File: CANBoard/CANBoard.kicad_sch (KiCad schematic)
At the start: 26 parts

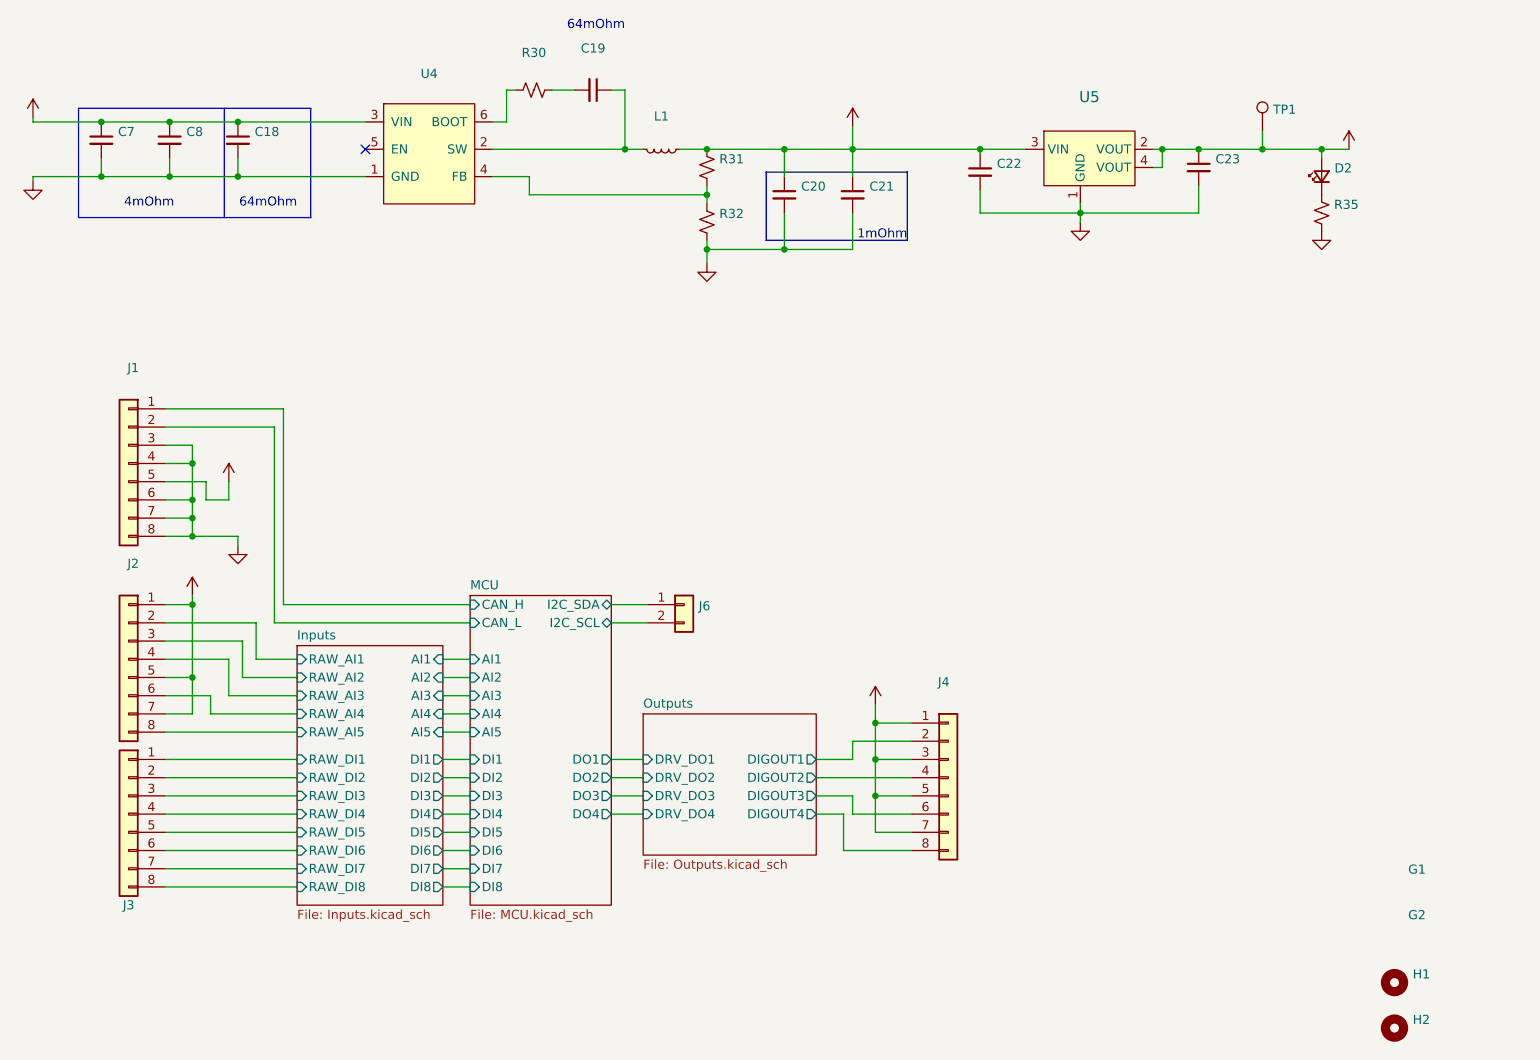
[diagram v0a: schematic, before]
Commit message: V2 updates
Removed FRAM, I2C and SWD pins. Added ID solder jumpers and Tag Connect
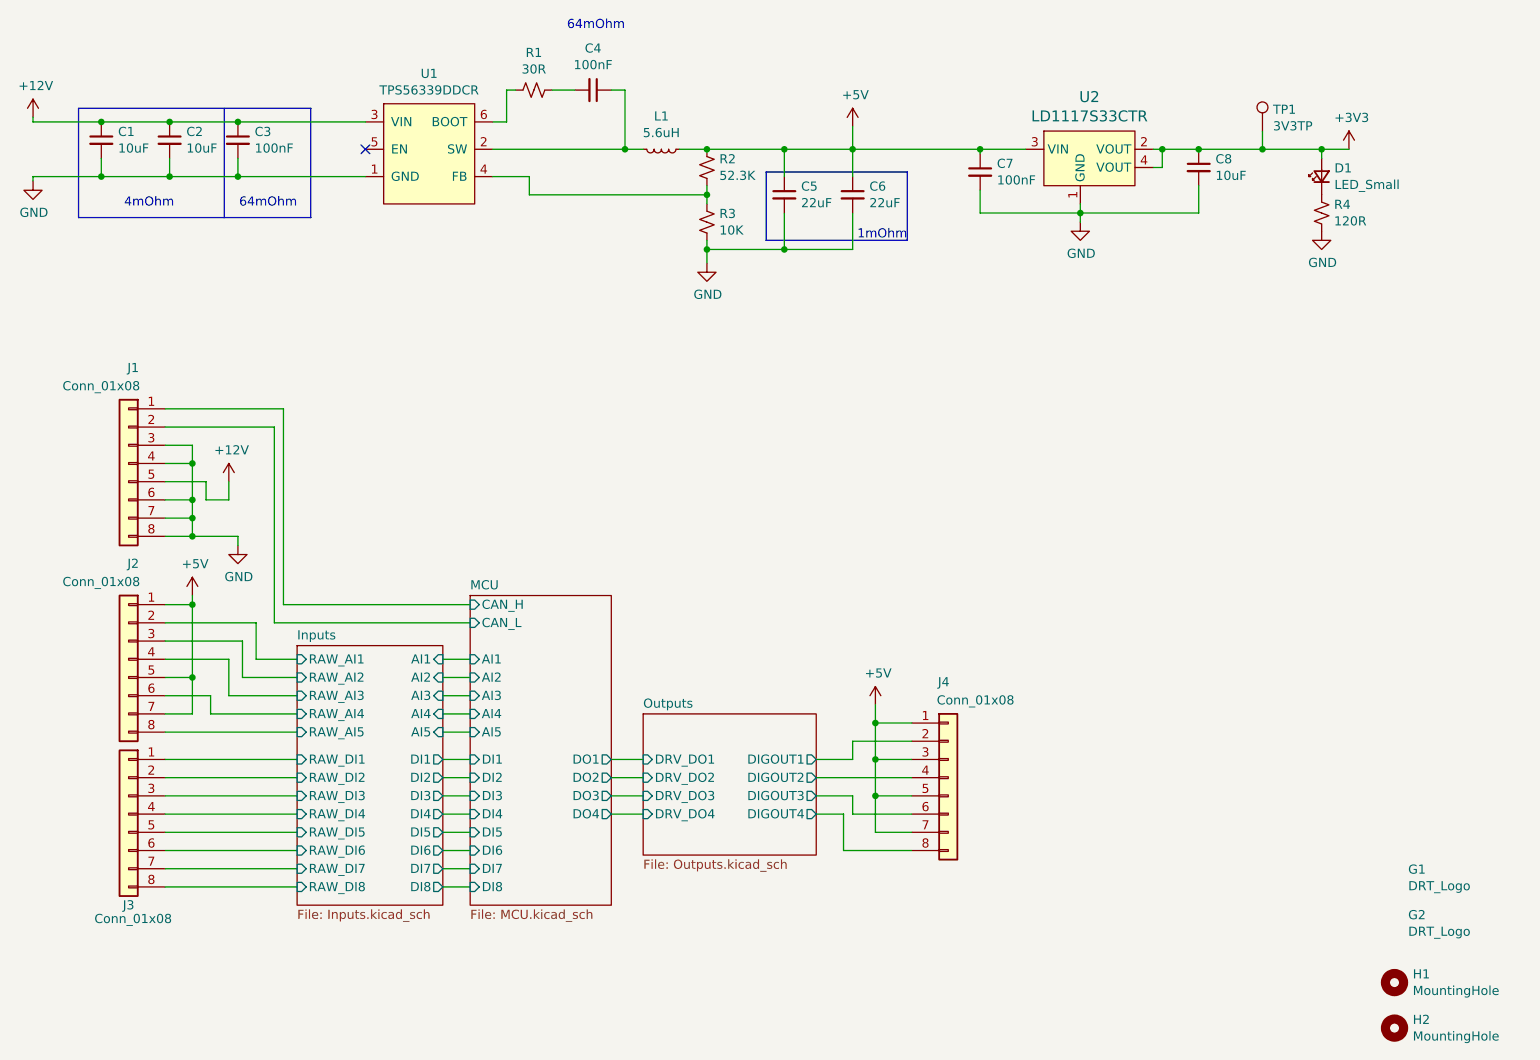
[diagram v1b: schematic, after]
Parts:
- removed J6: (no value), symbol Connector_Generic:Conn_01x02
- C1: renamed from C7; value (none) -> 10uF; footprint (none) -> Capacitor_SMD:C_0805_2012Metric
- C2: renamed from C8; value (none) -> 10uF; footprint (none) -> Capacitor_SMD:C_0805_2012Metric
- C3: renamed from C18; value (none) -> 100nF; footprint (none) -> Capacitor_SMD:C_0805_2012Metric
- C4: renamed from C19; value (none) -> 100nF; footprint (none) -> Capacitor_SMD:C_0805_2012Metric
- C5: renamed from C20; value (none) -> 22uF; footprint (none) -> Capacitor_SMD:C_0805_2012Metric
- C6: renamed from C21; value (none) -> 22uF; footprint (none) -> Capacitor_SMD:C_0805_2012Metric
- C7: renamed from C22; value (none) -> 100nF; footprint (none) -> Capacitor_SMD:C_0805_2012Metric
- C8: renamed from C23; value (none) -> 10uF; footprint (none) -> Capacitor_SMD:C_0805_2012Metric
- D1: renamed from D2; value (none) -> LED_Small; footprint (none) -> LED_SMD:LED_0805_2012Metric
- G1: value (none) -> DRT_Logo; footprint (none) -> DRTLogo:DRTLogo
- G2: value (none) -> DRT_Logo; footprint (none) -> DRTLogo:DingoFaceNoFill
- H1, H2: value (none) -> MountingHole; footprint (none) -> MountingHole:MountingHole_3.2mm_M3_DIN965_Pad
- J1, J2, J3, J4: value (none) -> Conn_01x08; footprint (none) -> Connector_PinHeader_2.54mm:PinHeader_1x08_P2.54mm_Vertical
- L1: value (none) -> 5.6uH; footprint (none) -> Inductors_SMD:Wuerth_LHMI
- R1: renamed from R30; value (none) -> 30R; footprint (none) -> Resistor_SMD:R_0805_2012Metric
- R2: renamed from R31; value (none) -> 52.3K; footprint (none) -> Resistor_SMD:R_0805_2012Metric
- R3: renamed from R32; value (none) -> 10K; footprint (none) -> Resistor_SMD:R_0805_2012Metric
- R4: renamed from R35; value (none) -> 120R; footprint (none) -> Resistor_SMD:R_0805_2012Metric
- TP1: value (none) -> 3V3TP; footprint (none) -> TestPoint:TestPoint_Pad_D1.0mm
- U1: renamed from U4; value (none) -> TPS56339DDCR; footprint (none) -> Package_TO_SOT_SMD:SOT-23-6
- U2: renamed from U5; value (none) -> LD1117S33CTR; footprint (none) -> digikey-footprints:SOT-223
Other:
- sheet MCU ports: added none; removed I2C_SCL, I2C_SDA

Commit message: Updated outputs, added JLCPCB LCSC part nums
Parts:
- C1, C2, C8: LCSC (none) -> C15850
- C3, C4, C7: LCSC (none) -> C49678
- C5, C6: LCSC (none) -> C45783
- D1: LCSC (none) -> C2900154
- L1: LCSC (none) -> C251691
- R1: LCSC (none) -> C325808
- R2: LCSC (none) -> C17740
- R3: LCSC (none) -> C17414
- R4: LCSC (none) -> C17437
- U1: LCSC (none) -> C2071106
- U2: LCSC (none) -> C35879
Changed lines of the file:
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@@
+      (effects (font (size 1.27 1.27)) hide)
+    )
+    (property "LCSC" "" (at 245.745 31.75 0)
       (effects (font (size 1.27 1.27)) hide)
     )
@@
       (effects (font (size 1.27 1.27)) hide)
     )
+    (property "LCSC" "" (at 265.43 135.89 0)
+      (effects (font (size 1.27 1.27)) hide)
+    )
     (instances
       (project "CANBoard"
@@
       (effects (font (size 1.27 1.27)) hide)
     )
+    (property "LCSC" "" (at 265.43 142.24 0)
+      (effects (font (size 1.27 1.27)) hide)
+    )
     (instances
       (project "CANBoard"
@@
       (effects (font (size 1.27 1.27)) hide)
     )
+    (property "LCSC" "" (at 264.16 150.495 0)
+      (effects (font (size 1.27 1.27)) hide)
+    )
     (instances
       (project "CANBoard"
@@
       (effects (font (size 1.27 1.27)) hide)
     )
+    (property "LCSC" "" (at 264.16 156.845 0)
+      (effects (font (size 1.27 1.27)) hide)
+    )
     (instances
       (project "CANBoard"
@@
     )
     (property "Datasheet" "~" (at 87.63 127 0)
+      (effects (font (size 1.27 1.27)) hide)
+    )
+    (property "LCSC" "" (at 87.63 127 0)
       (effects (font (size 1.27 1.27)) hide)
     )
@@
       (effects (font (size 1.27 1.27)) hide)
     )
+    (property "LCSC" "" (at 87.63 105.41 0)
+      (effects (font (size 1.27 1.27)) hide)
+    )
     (pin "1")
     (pin "2")
@@
       (effects (font (size 1.27 1.27)) hide)
     )
+    (property "LCSC" "" (at 201.93 121.92 0)
+      (effects (font (size 1.27 1.27)) hide)
+    )
     (pin "1")
     (pin "2")
@@
       (effects (font (size 1.27 1.27)) hide)
     )
+    (property "LCSC" "" (at 87.63 78.105 0)
+      (effects (font (size 1.27 1.27)) hide)
+    )
     (pin "1")
     (pin "2")
@@
       (effects (font (size 1.27 1.27)) hide)
     )
+    (property "LCSC" "C2900154" (at 254 38.1 0)
+      (effects (font (size 1.27 1.27)) hide)
+    )
     (pin "1")
     (pin "2")
@@
       (effects (font (size 1.27 1.27)) hide)
     )
+    (property "LCSC" "C17437" (at 254 43.18 0)
+      (effects (font (size 1.27 1.27)) hide)
+    )
     (pin "1")
     (pin "2")
@@
       (effects (font (size 1.27 1.27)) hide)
     )
+    (property "LCSC" "C251691" (at 161.925 34.29 0)
+      (effects (font (size 1.27 1.27)) hide)
+    )
     (pin "1")
     (pin "2")
@@
       (effects (font (size 1.27 1.27)) hide)
     )
+    (property "LCSC" "C15850" (at 93.345 33.02 0)
+      (effects (font (size 1.27 1.27)) hide)
+    )
     (pin "1")
     (pin "2")
@@
       (effects (font (size 1.27 1.27)) hide)
     )
+    (property "LCSC" "C49678" (at 102.87 33.02 0)
+      (effects (font (size 1.27 1.27)) hide)
+    )
     (pin "1")
     (pin "2")
@@
       (effects (font (size 1.27 1.27)) hide)
     )
+    (property "LCSC" "C325808" (at 144.145 26.035 0)
+      (effects (font (size 1.27 1.27)) hide)
+    )
     (pin "1")
     (pin "2")
@@
       (effects (font (size 1.27 1.27)) hide)
     )
+    (property "LCSC" "C49678" (at 152.4 26.035 0)
+      (effects (font (size 1.27 1.27)) hide)
+    )
     (pin "1")
     (pin "2")
@@
     )
     (property "Digi-Key_PN" "490-10748-1-ND" (at 83.82 33.02 0)
+      (effects (font (size 1.27 1.27)) hide)
+    )
+    (property "LCSC" "C15850" (at 83.82 33.02 0)
       (effects (font (size 1.27 1.27)) hide)
     )
@@
       (effects (font (size 1.27 1.27)) hide)
     )
+    (property "LCSC" "C17740" (at 168.275 36.83 0)
+      (effects (font (size 1.27 1.27)) hide)
+    )
     (pin "1")
     (pin "2")
@@
       (effects (font (size 1.27 1.27)) hide)
     )
+    (property "LCSC" "C17414" (at 168.275 44.45 0)
+      (effects (font (size 1.27 1.27)) hide)
+    )
     (pin "1")
     (pin "2")
@@
       (effects (font (size 1.27 1.27)) hide)
     )
+    (property "LCSC" "C45783" (at 179.07 40.64 0)
+      (effects (font (size 1.27 1.27)) hide)
+    )
     (pin "1")
     (pin "2")
@@
       (effects (font (size 1.27 1.27)) hide)
     )
+    (property "LCSC" "C45783" (at 188.595 40.64 0)
+      (effects (font (size 1.27 1.27)) hide)
+    )
     (pin "1")
     (pin "2")
@@
     )
     (property "Digi-Key_PN" "296-53568-1-ND" (at 129.54 34.29 0)
+      (effects (font (size 1.27 1.27)) hide)
+    )
+    (property "LCSC" "C2071106" (at 129.54 34.29 0)
       (effects (font (size 1.27 1.27)) hide)
     )
@@
       (effects (font (size 1.524 1.524)) (justify left) hide)
     )
+    (property "LCSC" "C35879" (at 220.345 34.29 0)
+      (effects (font (size 1.27 1.27)) hide)
+    )
     (pin "1")
     (pin "2")
@@
       (effects (font (size 1.27 1.27)) hide)
     )
+    (property "LCSC" "C49678" (at 206.375 37.465 0)
+      (effects (font (size 1.27 1.27)) hide)
+    )
     (pin "1")
     (pin "2")
@@
       (effects (font (size 1.27 1.27)) hide)
     )
+    (property "LCSC" "C15850" (at 236.855 36.83 0)
+      (effects (font (size 1.27 1.27)) hide)
+    )

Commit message: #12 Removed U1 EN pin 5, updated documentation
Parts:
- U1: footprint Package_TO_SOT_SMD:SOT-23-6 -> TO_SOT_SMD_Modify:SOT-23-6_NoPin5
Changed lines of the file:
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@@
       (effects (font (size 1.27 1.27)))
     )
-    (property "Footprint" "Package_TO_SOT_SMD:SOT-23-6" (at 129.54 30.48 0)
+    (property "Footprint" "TO_SOT_SMD_Modify:SOT-23-6_NoPin5" (at 129.54 30.48 0)
       (effects (font (size 1.27 1.27)) hide)
     )

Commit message: Updated JLC inductor part number
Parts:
- L1: LCSC C251691 -> C467062
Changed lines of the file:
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@@
       (effects (font (size 1.27 1.27)) hide)
     )
-    (property "LCSC" "C251691" (at 161.925 34.29 0)
+    (property "LCSC" "C467062" (at 161.925 34.29 0)
       (effects (font (size 1.27 1.27)) hide)
     )
